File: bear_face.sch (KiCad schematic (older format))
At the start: 195 parts, among them J1 USB_B_Micro, J2 Conn_02x03_Odd_Even, Q1 2N7002, SW1 SW_Push, U1 ATmega32U4-AU, U2 SRV05-4, Y1 16MHz

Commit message: Updated ESD tracking, edited footprints
Caps key footprint LED pads now support xd75 hotswap LED sockets
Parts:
- MX46: footprint MX_Only:MXOnly-1.75U -> bear_face_parts:MXOnly-1.75U-CapsLED-XD75-socket
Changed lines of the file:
@@
 F 0 "MX46" H 3733 3423 60  0000 C CNN
 F 1 "MX-NoLED" H 3733 3349 20  0000 C CNN
-F 2 "MX_Only:MXOnly-1.75U" H 3075 3175 60  0001 C CNN
+F 2 "bear_face_parts:MXOnly-1.75U-CapsLED-XD75-socket" H 3075 3175 60  0001 C CNN
 F 3 "" H 3075 3175 60  0001 C CNN
 	1    3700 3200

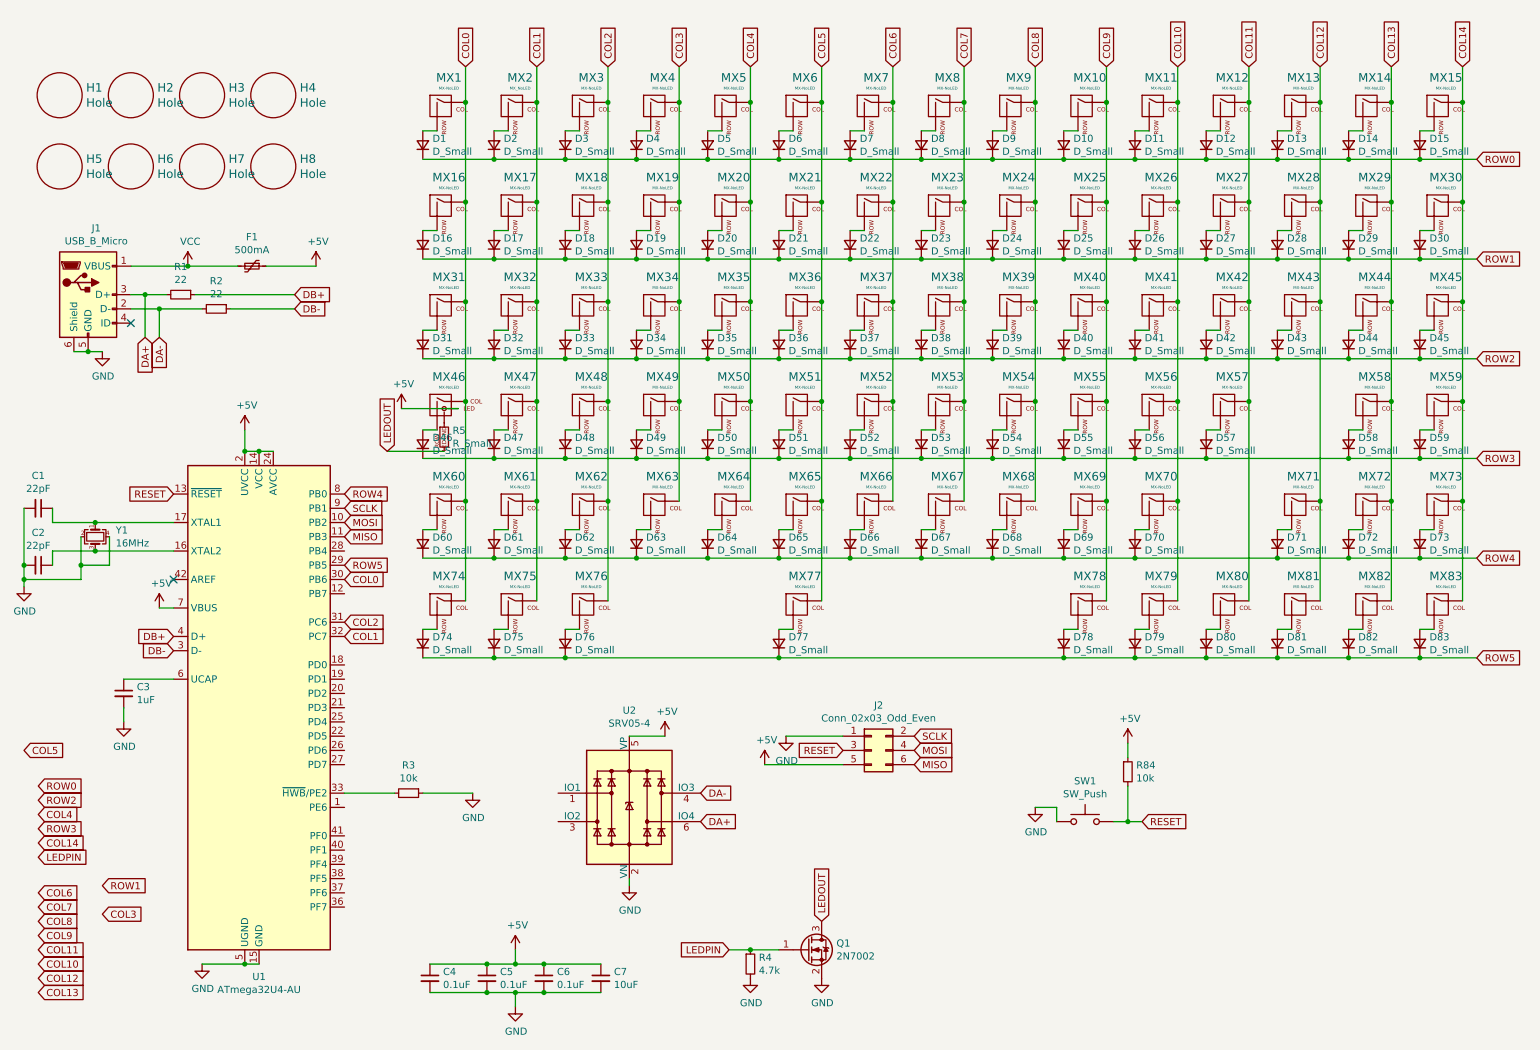
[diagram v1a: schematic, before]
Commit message: All nets routed, GND fill stitched, DRC passed
Ready for gerbers
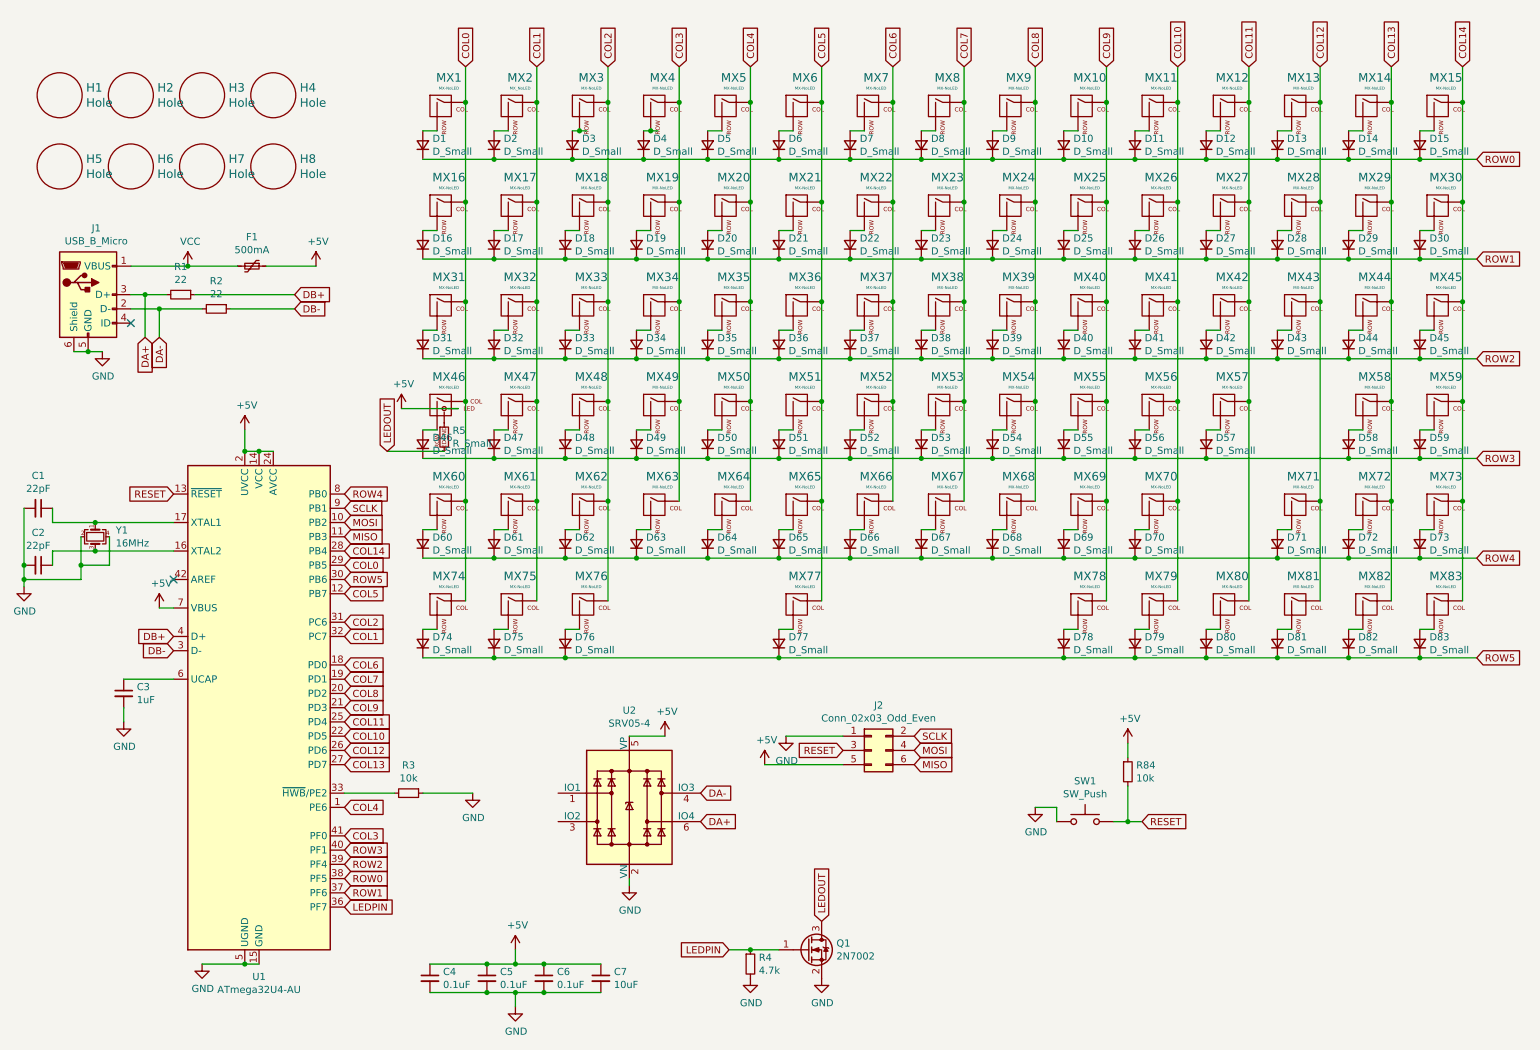
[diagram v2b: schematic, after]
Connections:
- net COL0: now also U1.29 (PB5); no longer U1.30 (PB6)
- net COL10: now also U1.22 (PD5)
- net COL11: now also U1.25 (PD4)
- net COL12: now also U1.26 (PD6)
- net COL13: now also U1.27 (PD7)
- net COL14: now also U1.28 (PB4)
- net COL3: now also U1.41 (PF0)
- net COL4: now also U1.1 (PE6)
- net COL5: now also U1.12 (PB7)
- net COL6: now also U1.18 (PD0)
- net COL7: now also U1.19 (PD1)
- net COL8: now also U1.20 (PD2)
- net COL9: now also U1.21 (PD3)
- net LEDPIN: now also U1.36 (PF7)
- net ROW0: now also U1.38 (PF5)
- net ROW1: now also U1.37 (PF6)
- net ROW2: now also U1.39 (PF4)
- net ROW3: now also U1.40 (PF1)
- net ROW5: now also U1.30 (PB6); no longer U1.29 (PB5)
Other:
- moved on the sheet: D3, D4
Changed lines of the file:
@@
 L Device:D_Small D3
 U 1 1 5DFC7643
-P 4550 1350
-F 0 "D3" V 4596 1282 50  0000 R CNN
-F 1 "D_Small" V 4505 1282 50  0000 R CNN
-F 2 "Keebio-Parts:Diode-dual" V 4550 1350 50  0001 C CNN
-F 3 "~" V 4550 1350 50  0001 C CNN
-	1    4550 1350
+P 4600 1350
+F 0 "D3" V 4646 1282 50  0000 R CNN
+F 1 "D_Small" V 4555 1282 50  0000 R CNN
+F 2 "Keebio-Parts:Diode-dual" V 4600 1350 50  0001 C CNN
+F 3 "~" V 4600 1350 50  0001 C CNN
+	1    4600 1350
 	0    -1   -1   0
 $EndComp
@@
 $EndComp
 Wire Wire Line
-	4550 1250 4650 1250
+	4600 1250 4650 1250
 $Comp
 L Device:D_Small D18
@@
 L Device:D_Small D4
 U 1 1 5DFFE01A
-P 5050 1350
-F 0 "D4" V 5096 1282 50  0000 R CNN
-F 1 "D_Small" V 5005 1282 50  0000 R CNN
-F 2 "Keebio-Parts:Diode-dual" V 5050 1350 50  0001 C CNN
-F 3 "~" V 5050 1350 50  0001 C CNN
-	1    5050 1350
-	0    -1   -1   0
-$EndComp
-Wire Wire Line
-	5050 1250 5150 1250
+P 5100 1350
+F 0 "D4" V 5146 1282 50  0000 R CNN
+F 1 "D_Small" V 5055 1282 50  0000 R CNN
+F 2 "Keebio-Parts:Diode-dual" V 5100 1350 50  0001 C CNN
+F 3 "~" V 5100 1350 50  0001 C CNN
+	1    5100 1350
+	0    -1   -1   0
+$EndComp
+Wire Wire Line
+	5100 1250 5150 1250
 Wire Wire Line
 	6050 1250 6150 1250
@@
 	3550 1450 4050 1450
 Connection ~ 4050 1450
-Wire Wire Line
-	4050 1450 4550 1450
-Connection ~ 4550 1450
-Wire Wire Line
-	4550 1450 5050 1450
-Connection ~ 5050 1450
-Wire Wire Line
-	5050 1450 5550 1450
 Connection ~ 5550 1450
 Wire Wire Line
@@
 Wire Wire Line
 	6350 4550 6350 3850
-Connection ~ 5350 1750
-Wire Wire Line
-	5350 1750 5350 1050
 Connection ~ 5350 2450
 Wire Wire Line
@@
 Wire Wire Line
 	5350 3850 5350 3150
-Wire Wire Line
-	4850 1050 4850 1750
-Connection ~ 4850 1750
 Wire Wire Line
 	4850 1750 4850 2450
@@
 Connection ~ 4350 1050
 Wire Wire Line
-	4850 1050 4850 800
-Connection ~ 4850 1050
-Wire Wire Line
 	5350 1050 5350 800
-Connection ~ 5350 1050
 Wire Wire Line
 	5850 1050 5850 800
@@
 	1    0    0    -1
 $EndComp
-Text GLabel 3000 4300 2    50   Input ~ 0
+Text GLabel 3000 4400 2    50   Input ~ 0
 ROW5
-Text GLabel 1300 6750 2    50   Input ~ 0
+Text GLabel 3000 6200 2    50   Input ~ 0
 COL3
 NoConn ~ 1800 4400
-Text GLabel 850  5850 2    50   Input ~ 0
+Text GLabel 3000 6500 2    50   Input ~ 0
 ROW0
-Text GLabel 1300 6550 2    50   Input ~ 0
+Text GLabel 3000 6600 2    50   Input ~ 0
 ROW1
-Text GLabel 850  5950 2    50   Input ~ 0
+Text GLabel 3000 6400 2    50   Input ~ 0
 ROW2
-Text GLabel 850  6150 2    50   Input ~ 0
+Text GLabel 3000 6300 2    50   Input ~ 0
 ROW3
-Text GLabel 750  5600 2    50   Input ~ 0
+Text GLabel 3000 4500 2    50   Input ~ 0
 COL5
-Text GLabel 850  6700 2    50   Input ~ 0
+Text GLabel 3000 5100 2    50   Input ~ 0
 COL7
-Text GLabel 850  6800 2    50   Input ~ 0
+Text GLabel 3000 5200 2    50   Input ~ 0
 COL8
-Text GLabel 850  6900 2    50   Input ~ 0
+Text GLabel 3000 5300 2    50   Input ~ 0
 COL9
-Text GLabel 850  7100 2    50   Input ~ 0
+Text GLabel 3000 5500 2    50   Input ~ 0
 COL10
-Text GLabel 850  7000 2    50   Input ~ 0
+Text GLabel 3000 5400 2    50   Input ~ 0
 COL11
-Text GLabel 850  7200 2    50   Input ~ 0
+Text GLabel 3000 5600 2    50   Input ~ 0
 COL12
-Text GLabel 850  7300 2    50   Input ~ 0
+Text GLabel 3000 5700 2    50   Input ~ 0
 COL13
-Text GLabel 850  6250 2    50   Input ~ 0
+Text GLabel 3000 4200 2    50   Input ~ 0
 COL14
-Text GLabel 850  6050 2    50   Input ~ 0
+Text GLabel 3000 6000 2    50   Input ~ 0
 COL4
-Text GLabel 850  6600 2    50   Input ~ 0
+Text GLabel 3000 5000 2    50   Input ~ 0
 COL6
 Text GLabel 3000 3800 2    50   Input ~ 0
@@
 Text GLabel 3000 4800 2    50   Input ~ 0
 COL1
-Text GLabel 3000 4400 2    50   Input ~ 0
+Text GLabel 3000 4300 2    50   Input ~ 0
 COL0
 NoConn ~ 1500 2600
-Text GLabel 850  6350 2    50   Input ~ 0
+Text GLabel 3000 6700 2    50   Input ~ 0
 LEDPIN
 Connection ~ 3850 3850
@@
 Text GLabel 3300 3500 1    50   Input ~ 0
 LEDOUT
+Connection ~ 4650 1250
+Wire Wire Line
+	4650 1250 4700 1250
+Connection ~ 5150 1250
+Wire Wire Line
+	5150 1250 5200 1250
+Connection ~ 4600 1450
+Connection ~ 5100 1450
+Wire Wire Line
+	5100 1450 5550 1450
+Wire Wire Line
+	4050 1450 4600 1450
+Wire Wire Line
+	4600 1450 5100 1450
+Wire Wire Line
+	4850 800  4850 1050
+Wire Wire Line
+	4850 1050 4850 1750
+Connection ~ 4850 1050
+Connection ~ 4850 1750
+Wire Wire Line
+	5350 1050 5350 1750
+Connection ~ 5350 1050
+Connection ~ 5350 1750
 $EndSCHEMATC

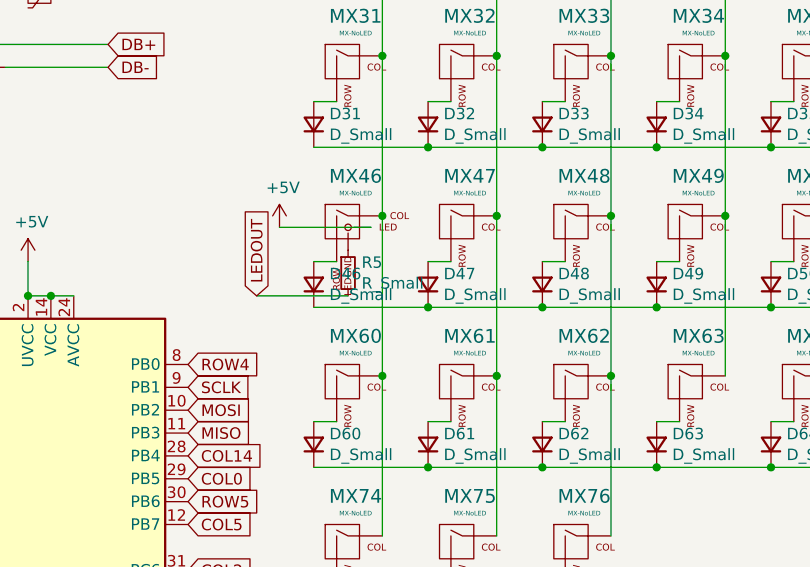
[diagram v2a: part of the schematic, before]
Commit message: Footprint SilkS updated
Component SilkS moved mostly to B.SilkS, reset switch and bootloader pins kept on Front
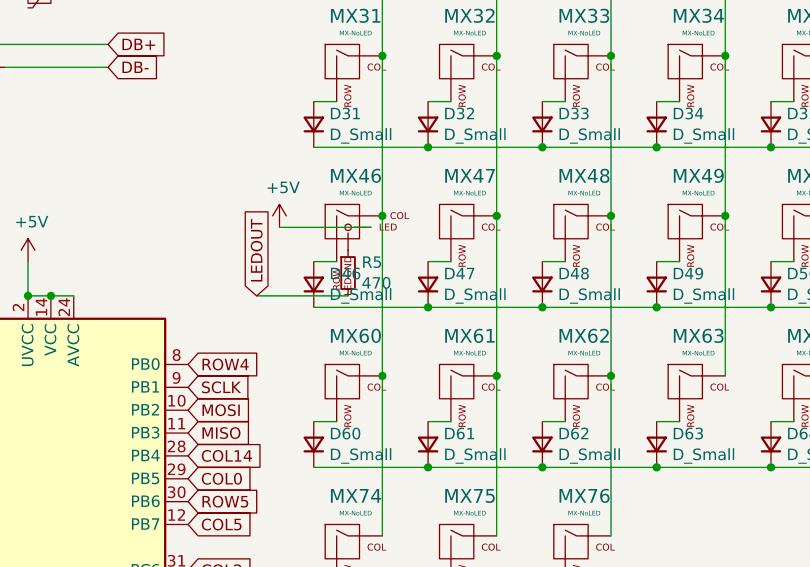
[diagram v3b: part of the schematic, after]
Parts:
- D1, D10, D11, D12, D13, D14, D15, D16, D17, D18, D19, D2, D20, D21, D22, D23, D24, D25, D26, D27, D28, D29, D3, D30, D31, D32, D33, D34, D35, D36, D37, D38, D39, D4, D40, D41, D42, D43, D44, D45, D46, D47, D48, D49, D5, D50, D51, D52, D53, D54, D55, D56, D57, D58, D59, D6, D60, D61, D62, D63, D64, D65, D66, D67, D68, D69, D7, D70, D71, D72, D73, D74, D75, D76, D77, D78, D79, D8, D80, D81, D82, D83, D9: footprint Keebio-Parts:Diode-dual -> bear_face_parts:Diode-Hybrid-Back
- R4: footprint Keebio-Parts:Resistor-Hybrid -> bear_face_parts:Resistor-Hybrid-Back
- R5: value R_Small -> 470; footprint Keebio-Parts:Resistor-Hybrid -> bear_face_parts:Resistor-Hybrid-Back

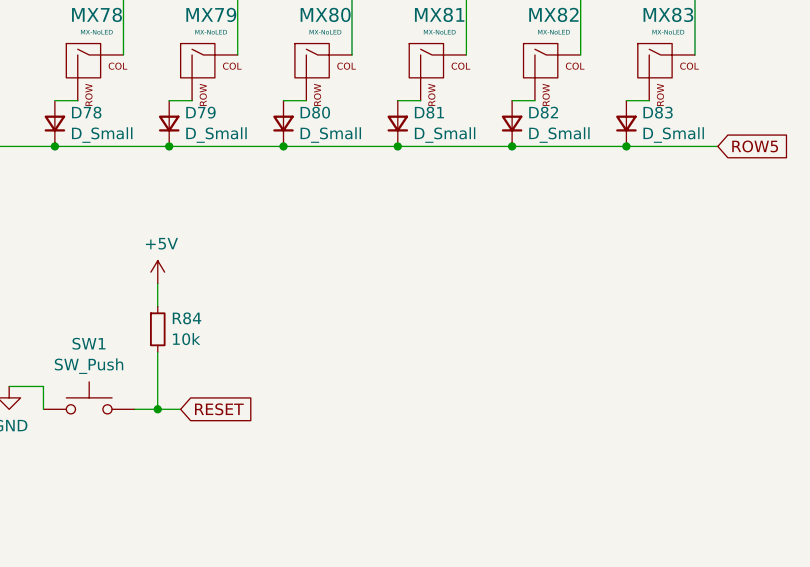
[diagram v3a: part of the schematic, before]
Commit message: Added decorations to .sch
No longer wiped by update from .sch
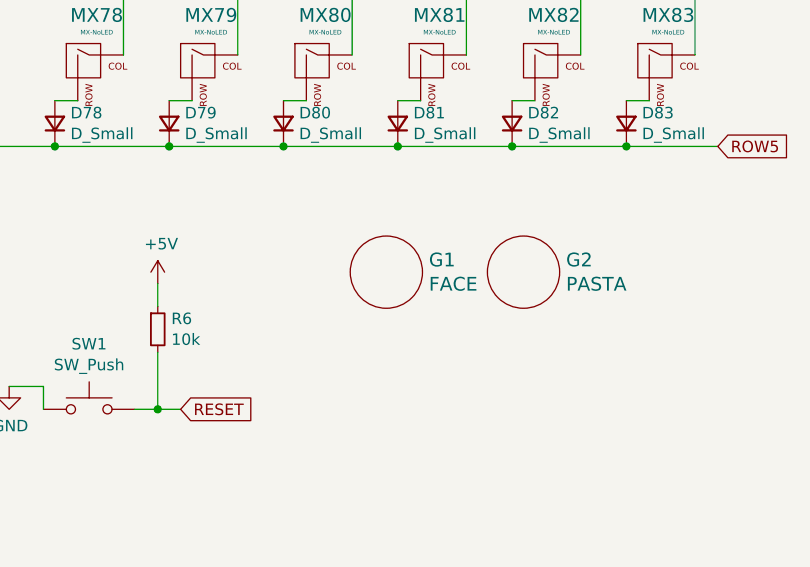
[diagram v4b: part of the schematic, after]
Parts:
- added G1: FACE, bear_face_silks:cbf_small_flipped, symbol keebio:Hole
- added G2: PASTA, bear_face_silks:pasta_small, symbol keebio:Hole
- renumbered R84 to R6
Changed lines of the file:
@@
 	8000 6000 8000 6100
 $Comp
-L Device:R_Small R84
+L Device:R_Small R6
 U 1 1 5E729BAE
 P 8500 5750
-F 0 "R84" H 8559 5796 50  0000 L CNN
+F 0 "R6" H 8559 5796 50  0000 L CNN
 F 1 "10k" H 8559 5705 50  0000 L CNN
 F 2 "Resistor_SMD:R_0805_2012Metric_Pad1.15x1.40mm_HandSolder" H 8500 5750 50  0001 C CNN
@@
 Connection ~ 5350 1050
 Connection ~ 5350 1750
+$Comp
+L keebio:Hole G1
+U 1 1 5E310D8F
+P 9500 5500
+F 0 "G1" H 9686 5553 60  0000 L CNN
+F 1 "FACE" H 9686 5447 60  0000 L CNN
+F 2 "bear_face_silks:cbf_small_flipped" H 9500 5500 60  0001 C CNN
+F 3 "" H 9500 5500 60  0001 C CNN
+	1    9500 5500
+	1    0    0    -1
+$EndComp
+$Comp
+L keebio:Hole G2
+U 1 1 5E3129DC
+P 10100 5500
+F 0 "G2" H 10286 5553 60  0000 L CNN
+F 1 "PASTA" H 10286 5447 60  0000 L CNN
+F 2 "bear_face_silks:pasta_small" H 10100 5500 60  0001 C CNN
+F 3 "" H 10100 5500 60  0001 C CNN
+	1    10100 5500
+	1    0    0    -1
+$EndComp
 $EndSCHEMATC
